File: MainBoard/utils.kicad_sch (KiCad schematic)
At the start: 22 parts, among them J2 Matrix_in, J3 Conn_01x02_Pin, Q1 AO3400A, Q2 AO3401A, Q3 PT1921C, Q4 PT1921C, U2 AT42QT1011-TSHR, U3 LIS3DH

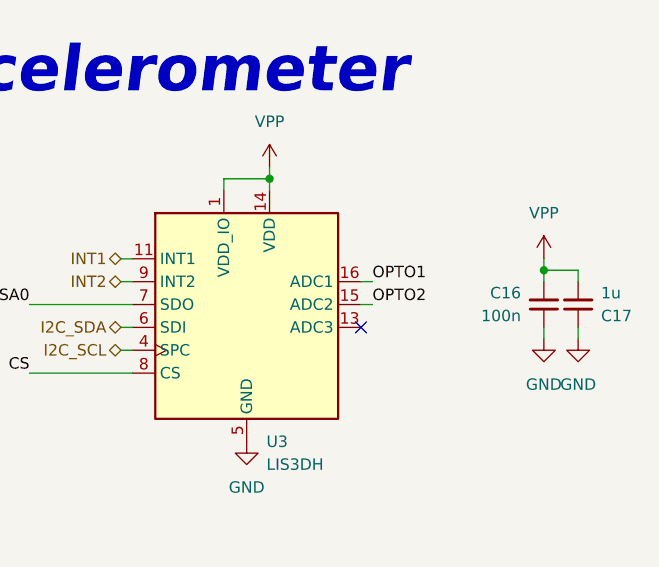
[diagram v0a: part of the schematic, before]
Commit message: Change some opto signals
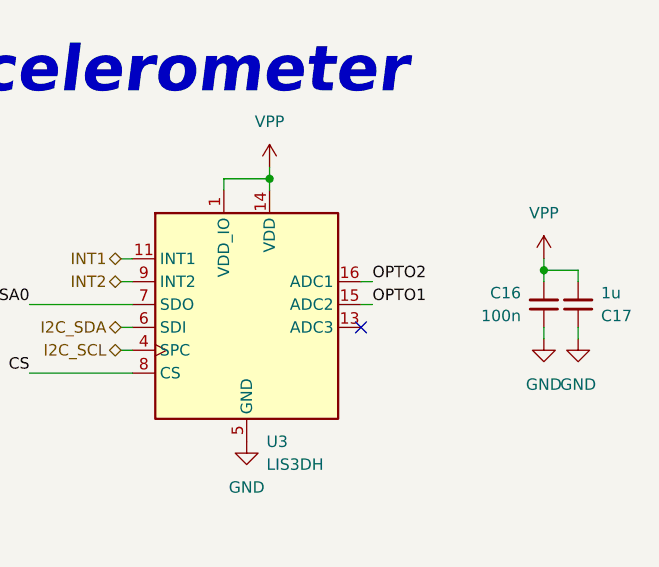
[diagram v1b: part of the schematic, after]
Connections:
- net OPTO1: now also U3.15 (ADC2); no longer U3.16 (ADC1)
- net OPTO2: now also U3.16 (ADC1); no longer U3.15 (ADC2)
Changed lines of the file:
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@@
 	)
 	(label "OPTO2"
-		(at 243.84 123.19 0)
+		(at 243.84 120.65 0)
 		(effects
 			(font
@@
 	)
 	(label "OPTO1"
-		(at 243.84 120.65 0)
+		(at 243.84 123.19 0)
 		(effects
 			(font
